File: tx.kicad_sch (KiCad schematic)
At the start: 58 parts, among them Q10 MMBF170, Q11 MMBF170, Q12 MMBF170, Q13 MMBF170, Q2 MMBF170, Q3 MMBF170, Q4 MMBF170, Q5 MMBF170, Q6 MMBF170, Q7 MMBF170, Q8 MMBF170, Q9 MMBF170, T1 BN-43-202_DualPri_CTSec, U4 ICE40UP5K-SG48ITR, U5 TLV70012, U6 CD74ACT541SM96

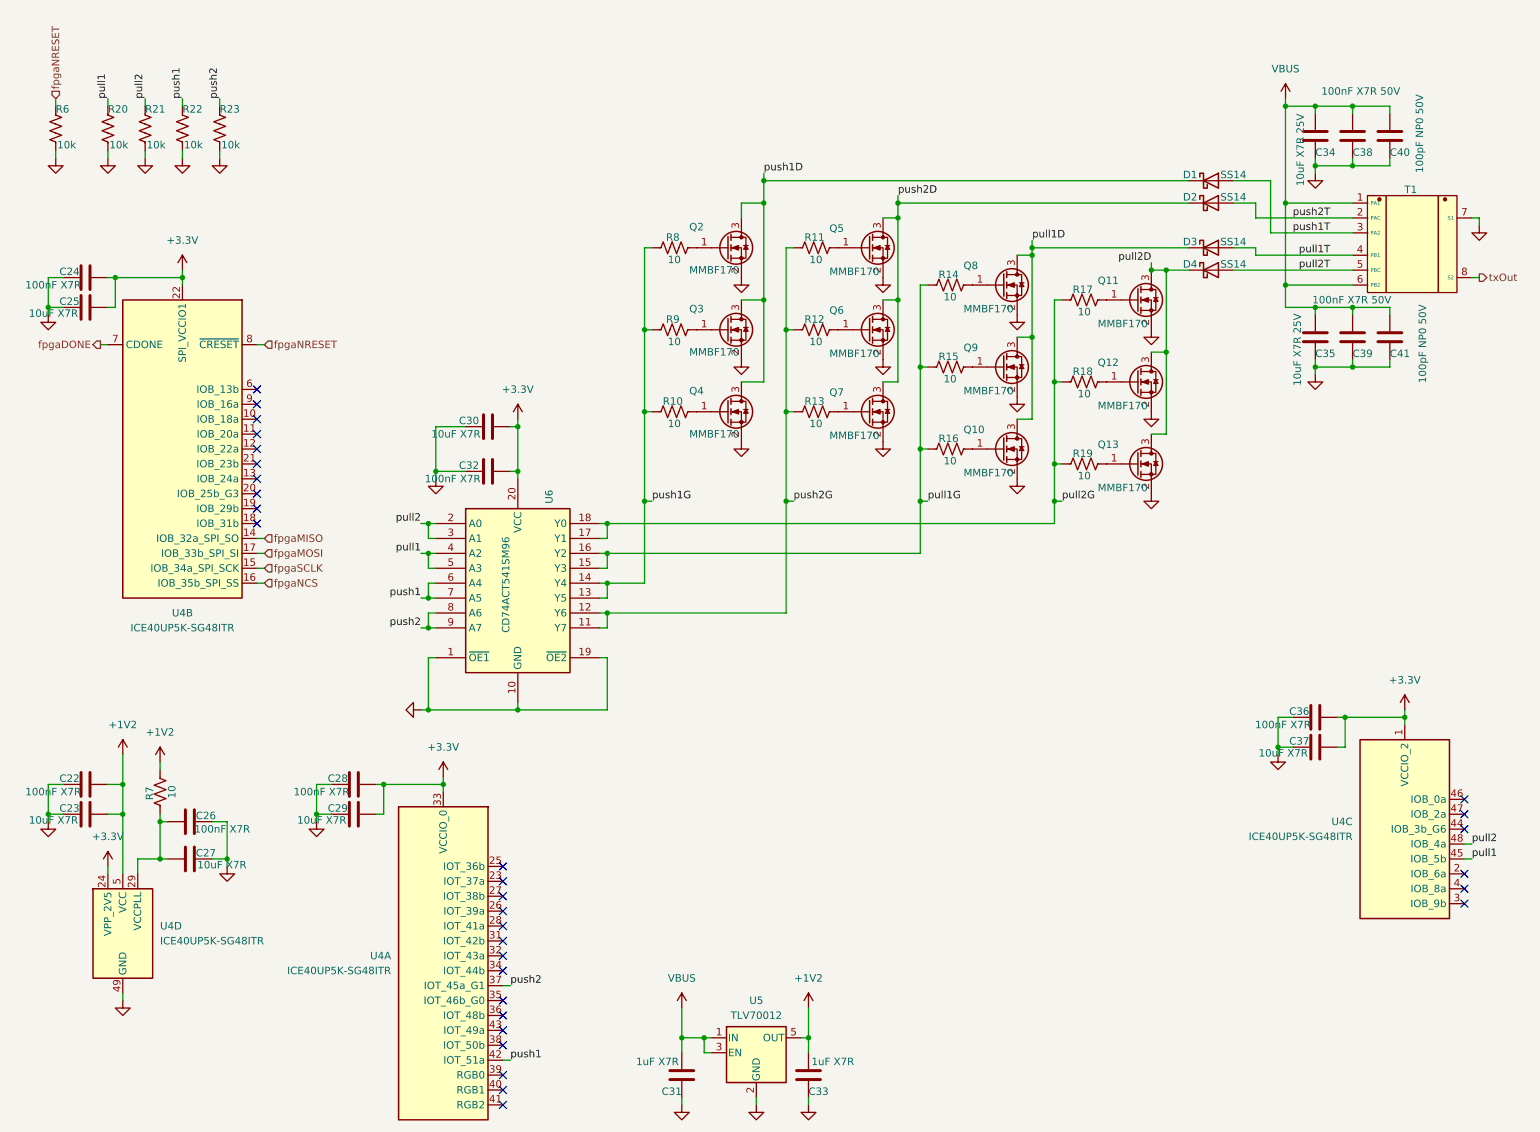
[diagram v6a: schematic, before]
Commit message: Fix up 3d in footprints in lib so they stay put when I update PCB from schematic. Fix text labels for same issue.
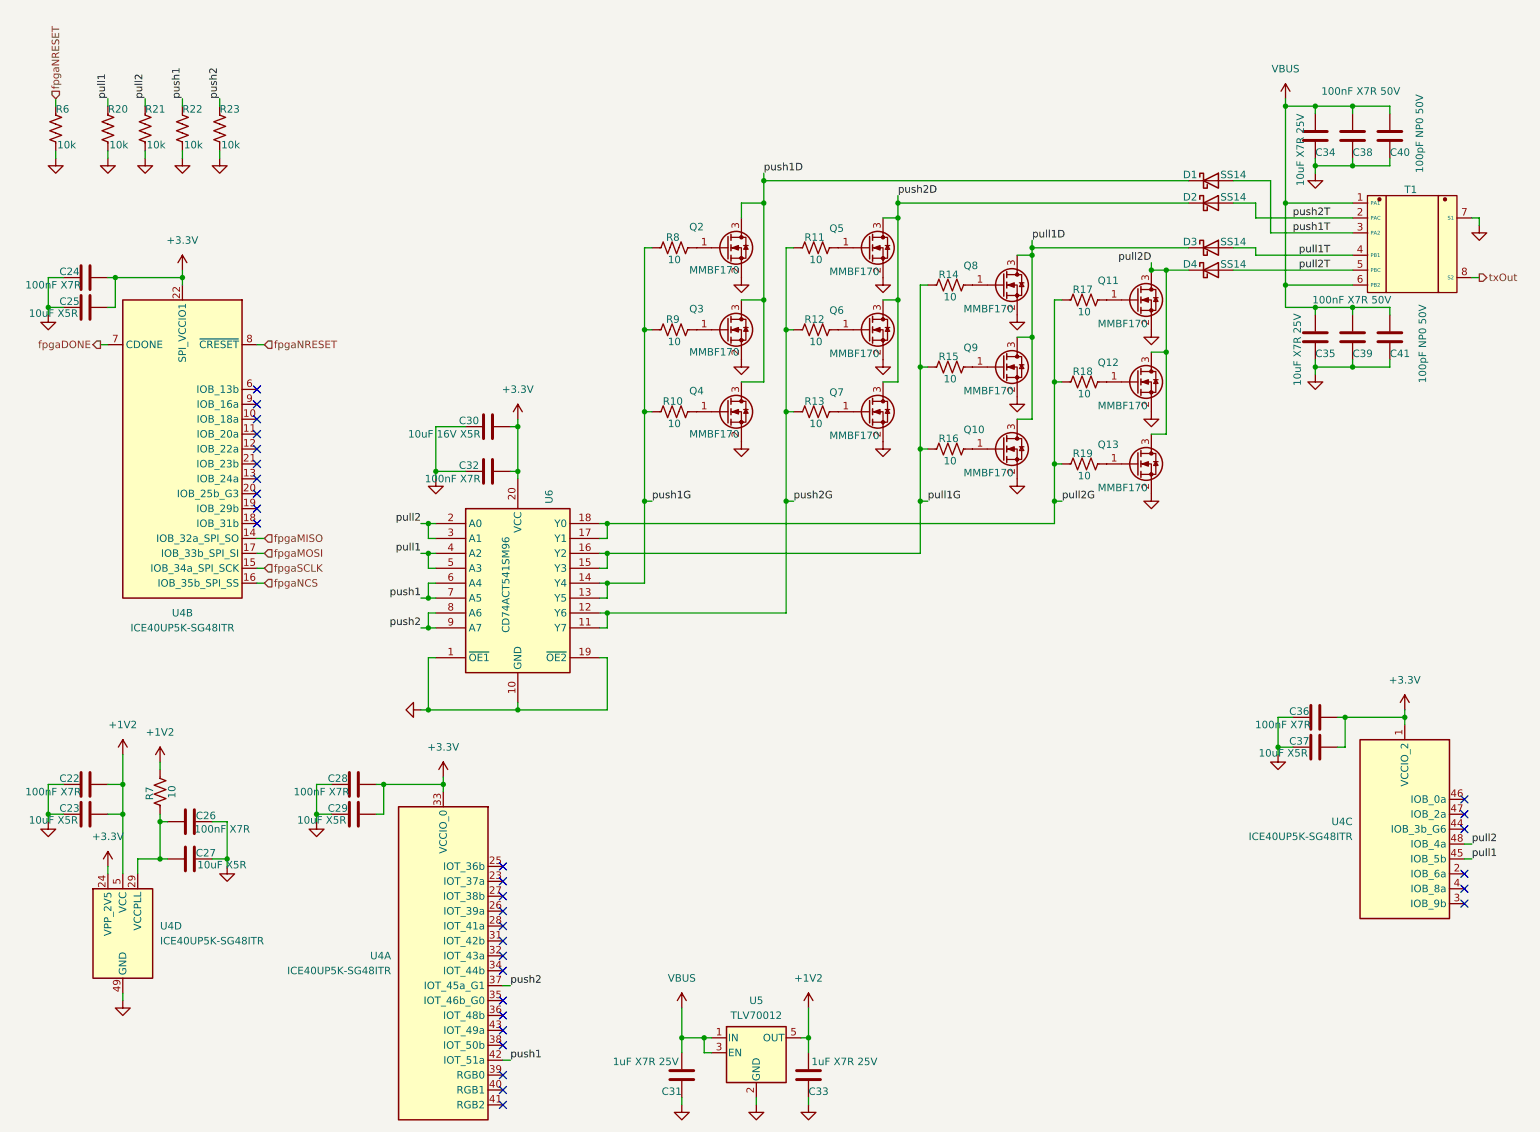
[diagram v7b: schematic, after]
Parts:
- C23, C25, C27, C29, C37: value 10uF X7R -> 10uF X5R; LCSC C2959727 -> C19702
- C30: value 10uF X7R -> 10uF 16V X5R; LCSC C32635 -> C1713
- C31, C33: value 1uF X7R -> 1uF X7R 25V
- U6: LCSC (none) -> C553178
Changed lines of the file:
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@@
 			)
 		)
+		(property "LCSC" "C553178"
+			(at 95.25 104.14 90)
+			(effects
+				(font
+					(size 1.27 1.27)
+				)
+				(hide yes)
+			)
+		)
 		(pin "16"
 		)
@@
 			)
 		)
-		(property "Value" "1uF X7R"
+		(property "Value" "1uF X7R 25V"
 			(at 145.288 190.754 0)
 			(effects
@@
 			)
 		)
-		(property "Value" "1uF X7R"
+		(property "Value" "1uF X7R 25V"
 			(at 122.682 190.754 0)
 			(effects
@@
 			)
 		)
-		(property "Value" "10uF X7R"
+		(property "Value" "10uF X5R"
 			(at 20.32 149.606 90)
 			(effects
@@
 			)
 		)
-		(property "LCSC" "C2959727"
+		(property "LCSC" "C19702"
 			(at 21.59 148.59 90)
 			(effects
@@
 			)
 		)
-		(property "Value" "10uF X7R"
+		(property "Value" "10uF X5R"
 			(at 40.64 157.226 90)
 			(effects
@@
 			)
 		)
-		(property "LCSC" "C2959727"
+		(property "LCSC" "C19702"
 			(at 39.37 156.21 90)
 			(effects
@@
 			)
 		)
-		(property "Value" "10uF X7R"
+		(property "Value" "10uF X5R"
 			(at 66.04 149.606 90)
 			(effects
@@
 			)
 		)
-		(property "LCSC" "C2959727"
+		(property "LCSC" "C19702"
 			(at 67.31 148.59 90)
 			(effects
@@
 			)
 		)
-		(property "Value" "10uF X7R"
+		(property "Value" "10uF X5R"
 			(at 20.32 63.246 90)
 			(effects
@@
 			)
 		)
-		(property "LCSC" "C2959727"
+		(property "LCSC" "C19702"
 			(at 21.59 62.23 90)
 			(effects
@@
 			)
 		)
-		(property "Value" "10uF X7R"
+		(property "Value" "10uF X5R"
 			(at 229.87 138.176 90)
 			(effects
@@
 			)
 		)
-		(property "LCSC" "C2959727"
+		(property "LCSC" "C19702"
 			(at 231.14 137.16 90)
 			(effects
@@
 			)
 		)
-		(property "Value" "10uF X7R"
+		(property "Value" "10uF 16V X5R"
 			(at 88.9 83.82 90)
 			(effects
@@
 			)
 		)
-		(property "LCSC" "C32635"
+		(property "LCSC" "C1713"
 			(at 90.17 82.55 0)
 			(effects

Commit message: Fixes to pass ERC. Nothing serious really.
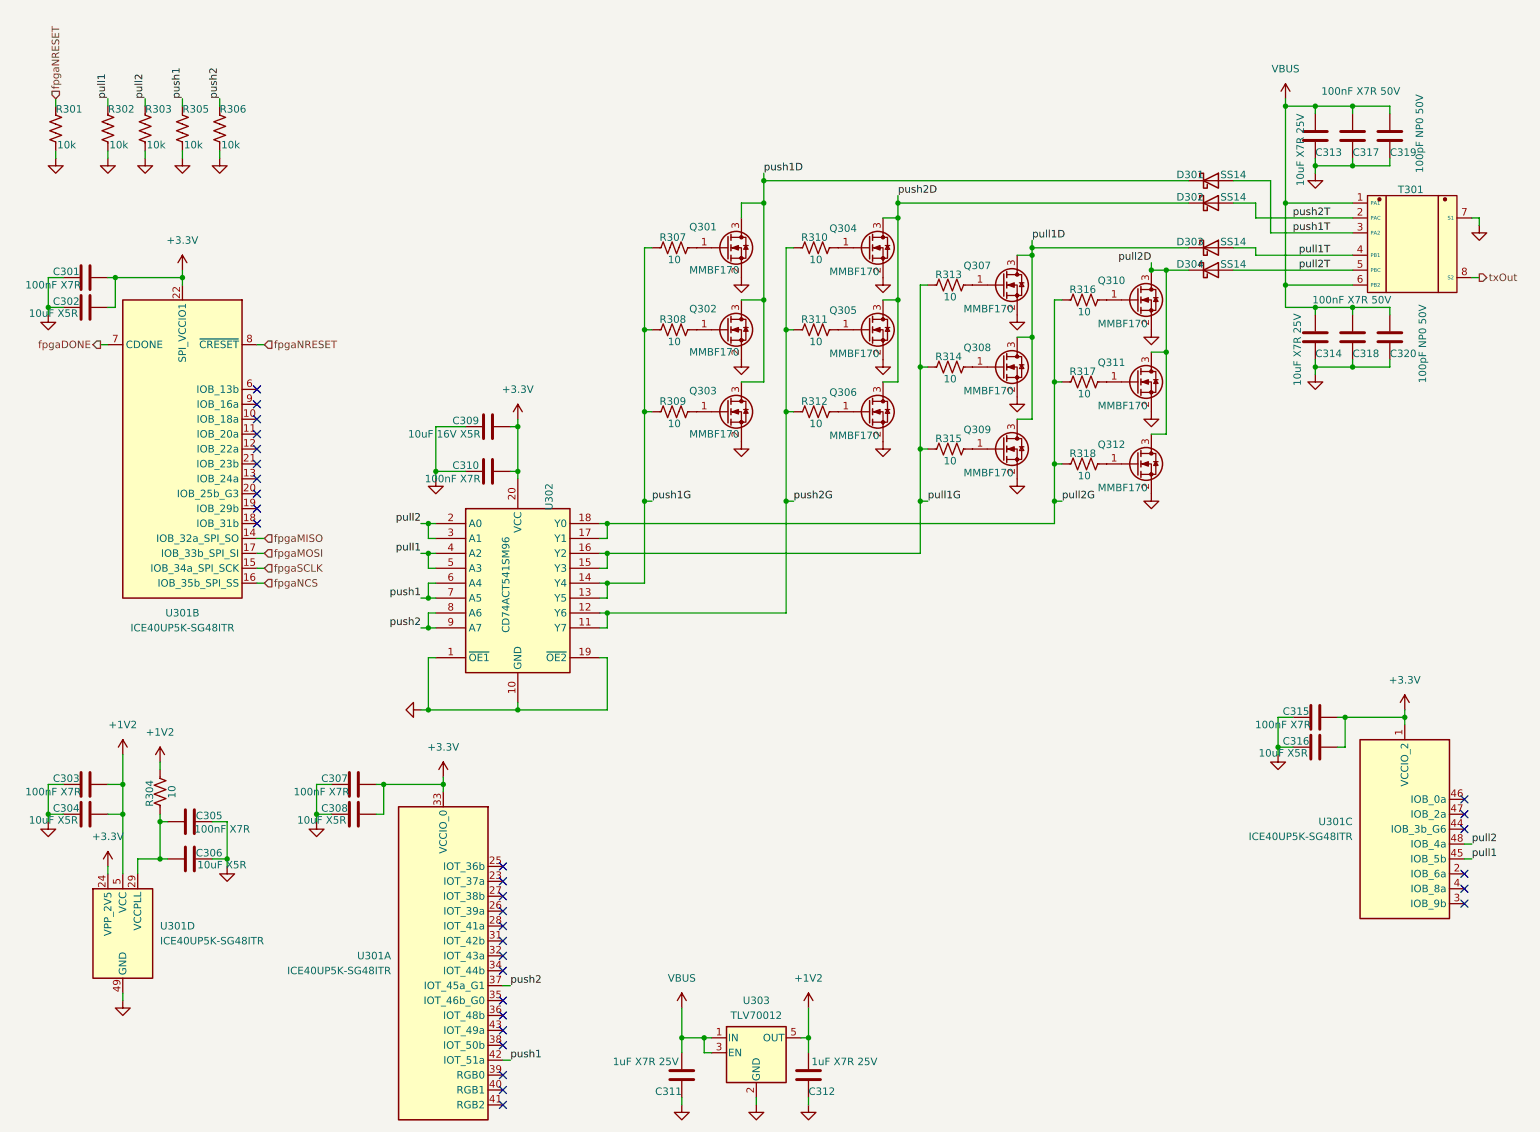
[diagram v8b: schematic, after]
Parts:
- renumbered C24 to C301, C25 to C302, C22 to C303, C23 to C304, C26 to C305, C27 to C306, C28 to C307, C29 to C308, C30 to C309, C32 to C310, C31 to C311, C33 to C312, C34 to C313, C35 to C314, C36 to C315, C37 to C316, C38 to C317, C39 to C318, C40 to C319, C41 to C320, D1 to D301, D2 to D302, D3 to D303, D4 to D304, Q2 to Q301, Q3 to Q302, Q4 to Q303, Q5 to Q304, Q6 to Q305, Q7 to Q306, Q8 to Q307, Q9 to Q308, Q10 to Q309, Q11 to Q310, Q12 to Q311, Q13 to Q312, R6 to R301, R20 to R302, R21 to R303, R7 to R304, R22 to R305, R23 to R306, R8 to R307, R9 to R308, R10 to R309, R11 to R310, R12 to R311, R13 to R312, R14 to R313, R15 to R314, R16 to R315, R17 to R316, R18 to R317, R19 to R318, T1 to T301, U4 to U301, U6 to U302, U5 to U303
